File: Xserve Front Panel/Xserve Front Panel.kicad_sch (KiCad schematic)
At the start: 48 parts

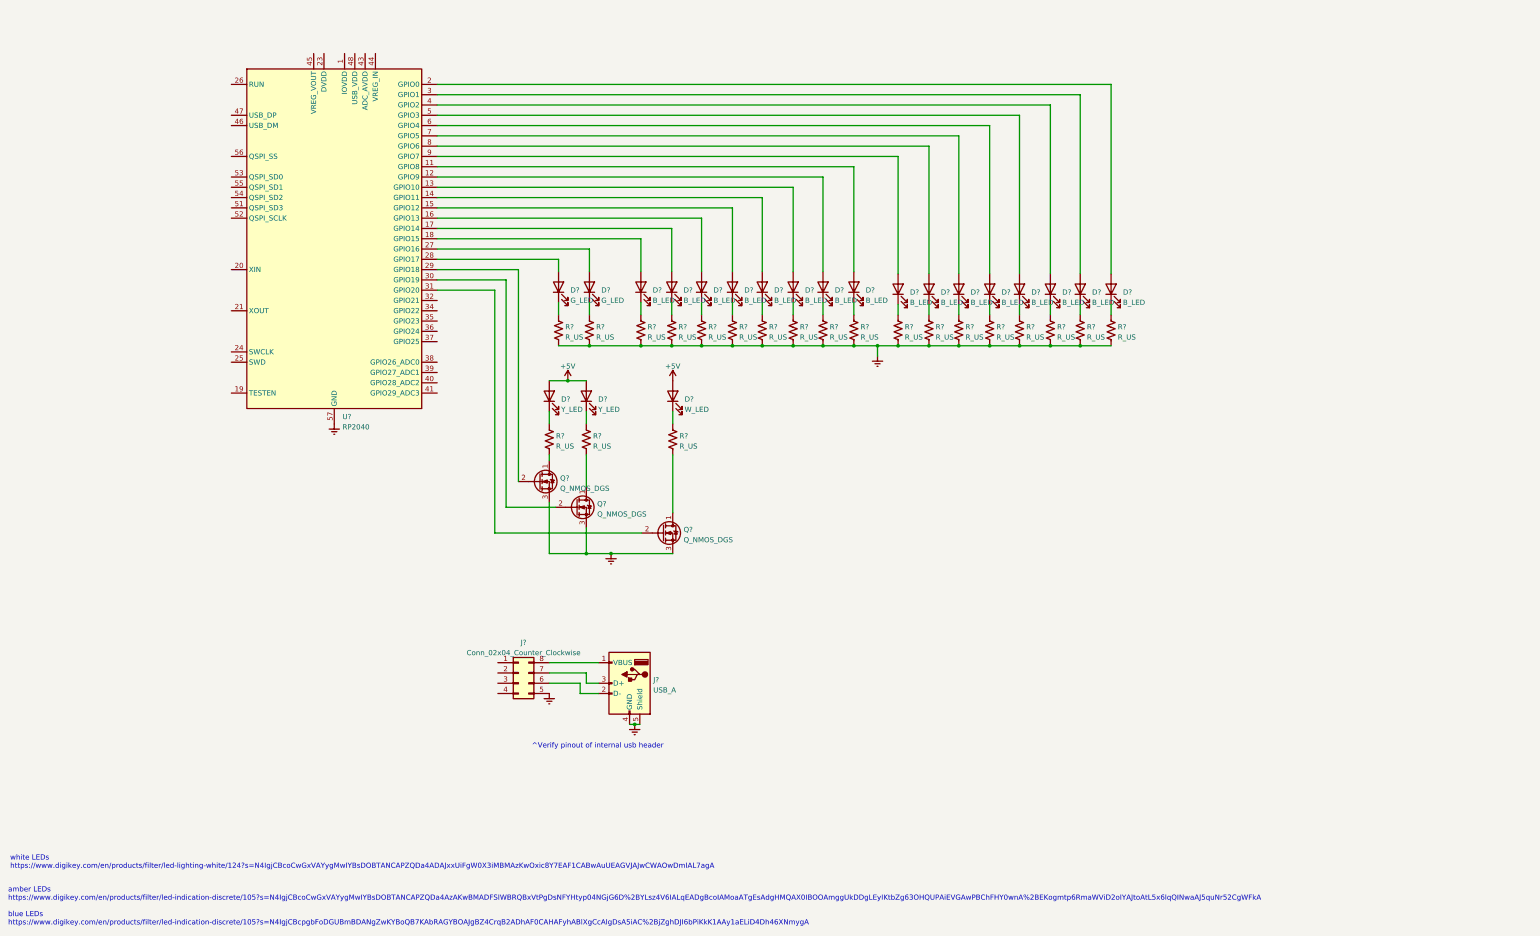
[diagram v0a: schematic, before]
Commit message: misinterpreted JLC's via size capabilities. increased minimum via to 0.46 mm to comply with their requirements.
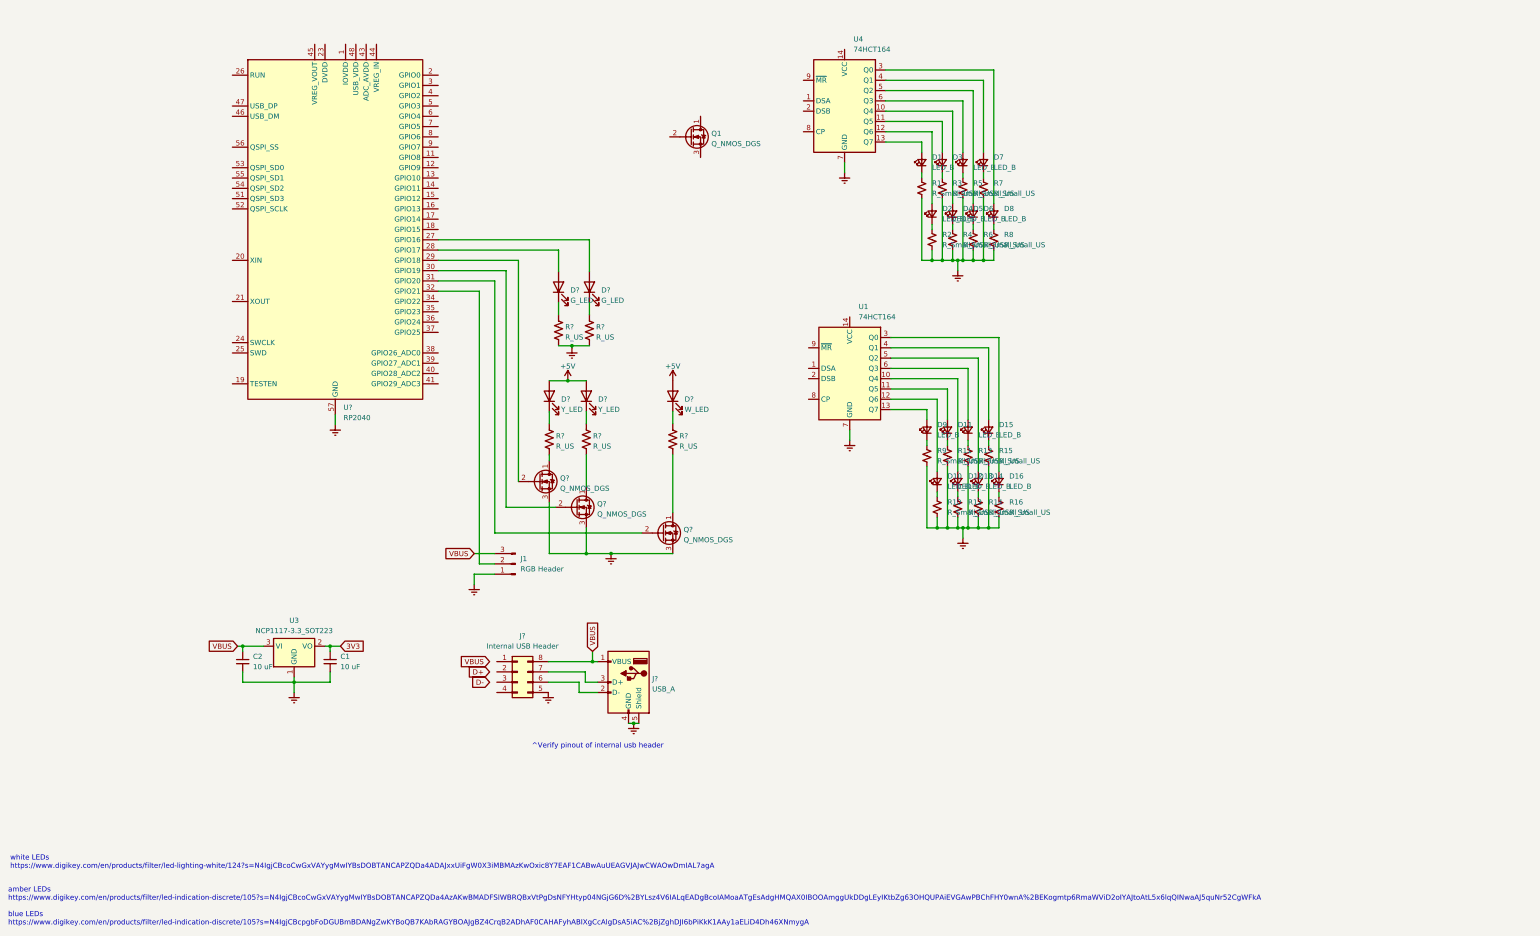
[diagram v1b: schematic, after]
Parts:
- removed D? (x16): B_LED, symbol Device:LED
- removed R? (x16): R_US, symbol Device:R_US
- added C1, C2: 10 uF, symbol Device:C_Small
- added D1, D10, D11, D12, D13, D14, D15, D16, D2, D3, D4, D5, D6, D7, D8, D9: LED_B, symbol Device:LED_Small
- added J1: RGB Header, symbol Connector:Conn_01x03_Pin
- added Q1: Q_NMOS_DGS, symbol Device:Q_NMOS_DGS
- added R1, R10, R11, R12, R13, R14, R15, R16, R2, R3, R4, R5, R6, R7, R8, R9: R_Small_US, symbol Device:R_Small_US
- added U1, U4: 74HCT164, symbol 74xx:74HCT164
- added U3: NCP1117-3.3_SOT223, Package_TO_SOT_SMD:SOT-223-3_TabPin2, symbol Regulator_Linear:NCP1117-3.3_SOT223
- J?: value Conn_02x04_Counter_Clockwise -> Internal USB Header
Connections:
- net Earth: now also C1.2, C2.2, J1.1 (Pin_1), R1.2, R10.2, R11.2, R12.2, R13.2, R14.2, R15.2, R16.2, R2.2, R3.2, R4.2, R5.2, R6.2, R7.2, R8.2, R9.2, U1.7 (GND), U3.1 (GND), U4.7 (GND)
- net VBUS: now reaches J?.1 (VBUS), J?.8 (Pin_8)
- net VBUS: now also C2.1, J1.3 (Pin_3), U3.3 (VI)
- net at U?.32 (GPIO21): now also J1.2 (Pin_2)
- new net: D2.1 (K), R2.1
- new net: D8.1 (K), R8.1
- new net: D5.1 (K), R5.1
- new net: D7.1 (K), R7.1
- new net: D7.2 (A), U4.4 (Q1)
- new net: D9.1 (K), R9.1
- new net: D14.1 (K), R14.1
- new net: D14.2 (A), U1.5 (Q2)
- new net: D10.1 (K), R10.1
- new net: D5.2 (A), U4.6 (Q3)
- new net: D1.1 (K), R1.1
- new net: D1.2 (A), U4.13 (Q7)
- new net: D4.1 (K), R4.1
- new net: D4.2 (A), U4.10 (Q4)
- new net: D3.1 (K), R3.1
- new net: D3.2 (A), U4.11 (Q5)
- new net: D6.1 (K), R6.1
- new net: D9.2 (A), U1.13 (Q7)
- new net: D12.1 (K), R12.1
- new net: D12.2 (A), U1.10 (Q4)
- new net: D8.2 (A), U4.3 (Q0)
- new net: D6.2 (A), U4.5 (Q2)
- new net: D15.1 (K), R15.1
- new net: D15.2 (A), U1.4 (Q1)
- new net: D13.1 (K), R13.1
- new net: D11.2 (A), U1.11 (Q5)
- new net: D10.2 (A), U1.12 (Q6)
- new net: D16.2 (A), U1.3 (Q0)
- new net: D13.2 (A), U1.6 (Q3)
- new net: D11.1 (K), R11.1
- new net: D2.2 (A), U4.12 (Q6)
- new net: D16.1 (K), R16.1
- new net 3V3: C1.1, U3.2 (VO)
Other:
- moved on the sheet: U?

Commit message: got the front panel PCB schematic to a decent place. Just need to fill in the details (all the passive values, maybe add some fuses, clean up the schematic).
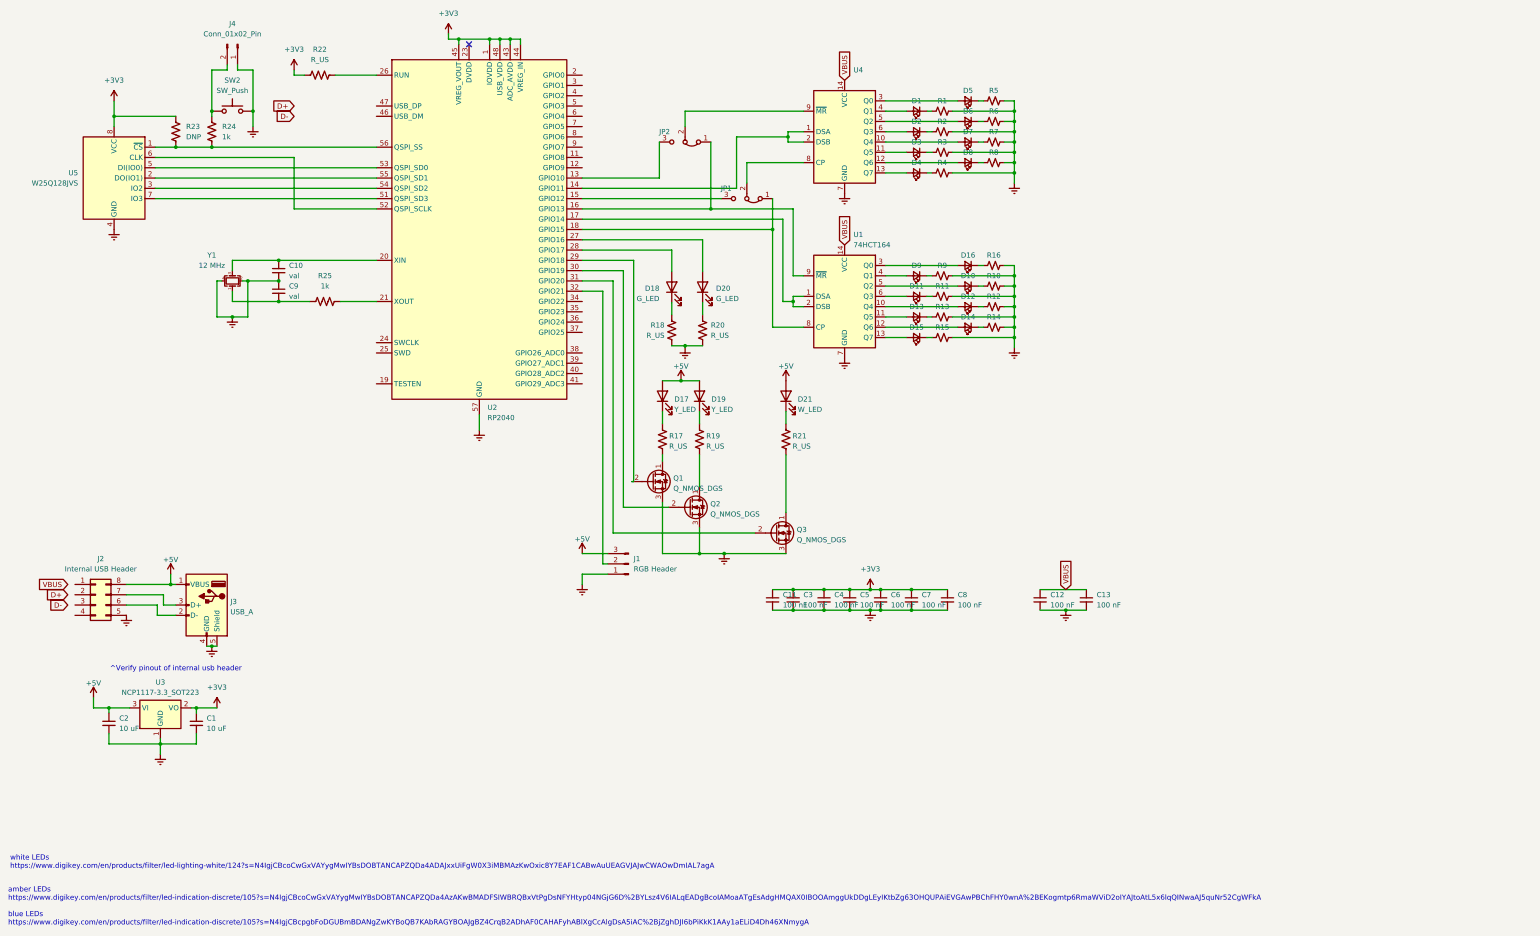
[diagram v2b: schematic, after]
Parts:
- removed Q1: Q_NMOS_DGS, symbol Device:Q_NMOS_DGS
- added C10, C9: val, symbol Device:C_Small
- added C11, C12, C13, C3, C4, C5, C6, C7, C8: 100 nF, symbol Device:C_Small
- added J4: Conn_01x02_Pin, symbol Connector:Conn_01x02_Pin
- added JP1, JP2: Jumper_3_Bridged12, symbol Jumper:Jumper_3_Bridged12
- added R22: R_US, symbol Device:R_US
- added R23: DNP, symbol Device:R_US
- added R24, R25: 1k, symbol Device:R_US
- added SW2: SW_Push, symbol Switch:SW_Push
- added U5: W25Q128JVS, Package_SO:SOIC-8_5.23x5.23mm_P1.27mm, symbol Memory_Flash:W25Q128JVS
- added Y1: 12 MHz, symbol Device:Crystal_GND24_Small
- D1, D10, D11, D12, D13, D14, D15, D16, D2, D3, D4, D5, D6, D7, D8, D9: footprint (none) -> LED_SMD:LED_0603_1608Metric_Pad1.05x0.95mm_HandSolder
- R1, R10, R11, R12, R13, R14, R15, R16, R2, R3, R4, R5, R6, R7, R8, R9: footprint (none) -> Resistor_SMD:R_0603_1608Metric_Pad0.98x0.95mm_HandSolder
- gave numbers to parts that had none: 16
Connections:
- net 3V3 is gone; now on net +3V3: C1.1, U3.2 (VO)
- net +5V: now also C2.1, J1.3 (Pin_3), J2.8 (Pin_8), J3.1 (VBUS), U3.3 (VI)
- net Earth: now also C10.2, C11.2, C12.2, C13.2, C3.2, C4.2, C5.2, C6.2, C7.2, C8.2, C9.1, J4.1 (Pin_1), SW2.2, U5.4 (GND), Y1.2, Y1.4
- net VBUS: now also U1.14 (VCC), U4.14 (VCC), C12.1, C13.1; no longer C2.1, J1.3 (Pin_3), J2.8 (Pin_8), J3.1 (VBUS), U3.3 (VI)
- net at U4.4 (Q1): now also D1.2 (A); no longer D7.2 (A)
- net at D14.2 (A): now also U1.12 (Q6); no longer U1.5 (Q2)
- net at D5.2 (A): now also U4.3 (Q0); no longer U4.6 (Q3)
- net at U4.13 (Q7): now also D4.2 (A); no longer D1.2 (A)
- net at U4.10 (Q4): now also D7.2 (A); no longer D4.2 (A)
- net at D9.2 (A): now also U1.4 (Q1); no longer U1.13 (Q7)
- net at D8.2 (A): now also U4.12 (Q6); no longer U4.3 (Q0)
- net at D15.2 (A): now also U1.13 (Q7); no longer U1.4 (Q1)
- net at U1.1 (DSA): now also U1.2 (DSB), U2.17 (GPIO14)
- net at U1.11 (Q5): now also D13.2 (A); no longer D11.2 (A)
- net at D10.2 (A): now also U1.5 (Q2); no longer U1.12 (Q6)
- net at U1.6 (Q3): now also D11.2 (A); no longer D13.2 (A)
- net at U1.8 (CP): now also U2.18 (GPIO15), JP1.1 (A)
- net at U1.9 (~{MR}): now also U2.16 (GPIO13), JP2.1 (A)
- net at U4.1 (DSA): now also U2.14 (GPIO11), U4.2 (DSB)
- net at D2.2 (A): now also U4.6 (Q3); no longer U4.12 (Q6)
- net at U4.8 (CP): now also JP1.2 (C)
- net at U4.9 (~{MR}): now also JP2.2 (C)
- net +3V3: now reaches U2.1 (IOVDD), U2.10 (IOVDD), U2.22 (IOVDD), U2.33 (IOVDD), U2.42 (IOVDD), U2.49 (IOVDD)
- net +3V3: now also U2.43 (ADC_AVDD), U2.44 (VREG_IN), U2.45 (VREG_VOUT), U2.48 (USB_VDD), C11.1, C3.1, C4.1, C5.1, C6.1, C7.1, C8.1, R22.1, R23.2, U5.8 (VCC)
- net at U2.13 (GPIO10): now also JP2.3 (B)
- net at U2.15 (GPIO12): now also JP1.3 (B)
- net at U2.20 (XIN): now also C10.1, Y1.3
- net at U2.21 (XOUT): now also R25.2
- net at U2.26 (RUN): now also R22.2
- net at U2.51 (QSPI_SD3): now also U5.7 (IO3)
- net at U2.52 (QSPI_SCLK): now also U5.6 (CLK)
- net at U2.53 (QSPI_SD0): now also U5.5 (DI(IO0))
- net at U2.54 (QSPI_SD2): now also U5.3 (IO2)
- net at U2.55 (QSPI_SD1): now also U5.2 (DO(IO1))
- net at U2.56 (QSPI_SS): now also R23.1, R24.1, U5.1 (~{CS})
- new net: J4.2 (Pin_2), R24.2, SW2.1
- new net: C9.2, R25.1, Y1.1
- no-connect marks 0 -> 1
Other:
- moved on the sheet: C1, C2, D16, D17, D18, D19, D20, D21, J1, J2, J3, Q1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

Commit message: Incremental changes, not exactly sure what's in this commit but thought it best to commit.
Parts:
- removed J2: Internal USB Header, symbol Connector_Generic:Conn_02x04_Counter_Clockwise
- added F1, F2: Polyfuse_Small, Fuse:Fuse_1206_3216Metric_Pad1.42x1.75mm_HandSolder, symbol Device:Polyfuse_Small
- added J6: Conn_02x05_Odd_Even, Connector_PinHeader_2.54mm:PinHeader_1x10_P2.54mm_Horizontal, symbol Connector_Generic:Conn_02x05_Odd_Even
- added R26, R27: R_US, Resistor_SMD:R_0603_1608Metric_Pad0.98x0.95mm_HandSolder, symbol Device:R_US
- C1, C10, C11, C12, C13, C2, C3, C4, C5, C6, C7, C8, C9: footprint (none) -> Capacitor_SMD:C_0603_1608Metric_Pad1.08x0.95mm_HandSolder
- D17, D18, D19, D20: footprint (none) -> LED_SMD:LED_0603_1608Metric_Pad1.05x0.95mm_HandSolder
- J1: footprint (none) -> Connector_PinHeader_2.54mm:PinHeader_1x03_P2.54mm_Horizontal
- J3: footprint (none) -> Connector_USB:USB_A_Molex_67643_Horizontal
- J4: footprint (none) -> Connector_PinHeader_2.54mm:PinHeader_1x02_P2.54mm_Vertical
- JP1, JP2: footprint (none) -> Jumper:SolderJumper-3_P1.3mm_Bridged2Bar12_Pad1.0x1.5mm_NumberLabels
- Q1, Q2, Q3: footprint (none) -> Package_TO_SOT_SMD:SOT-23_Handsoldering
- R17, R18, R19, R20, R21, R22, R23, R24, R25: footprint (none) -> Resistor_SMD:R_0603_1608Metric_Pad0.98x0.95mm_HandSolder
- SW2: footprint (none) -> Button_Switch_THT:SW_TH_Tactile_Omron_B3F-10xx
- U1, U4: footprint (none) -> Package_SO:SO-14_3.9x8.65mm_P1.27mm
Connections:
- net VBUS is gone; now on net +5V: C12.1, C13.1, U1.14 (VCC), U4.14 (VCC)
- net +5V: now also F2.1; no longer J3.1 (VBUS)
- net D+: now also J6.5 (Pin_5), R26.1
- net D-: now also J6.3 (Pin_3), R27.1
- net Earth: now also J6.7 (Pin_7), J6.8 (Pin_8)
- net at J3.2 (D-): now also J6.4 (Pin_4)
- net at J3.3 (D+): now also J6.6 (Pin_6)
- net at U2.46 (USB_DM): now also R27.2
- net at U2.47 (USB_DP): now also R26.2
- new net: F2.2, J6.1 (Pin_1)
- new net: F1.1, J6.2 (Pin_2)
- new net: F1.2, J3.1 (VBUS)
- no-connect marks 1 -> 3
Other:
- note removed: "^Verify pinout of internal usb header"
- moved on the sheet: C1, C2, J3, U3
